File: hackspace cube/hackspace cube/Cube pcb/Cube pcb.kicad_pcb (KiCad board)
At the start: 2 copper layers, 57 parts, among them J1 Conn_01x08 ( conector 1), J2 Conn_01x08 ( conector 2), J3 Conn_01x02 ( exstra ground co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, J4 Conn_01x14 ( Spare Ports ), Q1 BSS138, Q10 BSS138, Q11 BSS138, Q12 BSS138, Q13 BSS138, Q14 BSS138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

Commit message: updating pcb
updating pcb most pins attached
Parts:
- moved C2 126.9 mm to (170.4, 108.5), turned to 180 degrees
- moved C1 122.3 mm to (166.1, 108.5)
- moved R24 101.7 mm to (139.7, 125.0)
- moved R23 100.9 mm to (139.7, 114.5)
- moved R22 97.3 mm to (134.2, 125.0)
- moved R21 96.5 mm to (134.7, 114.5)
- moved R20 93.8 mm to (129.2, 125.0)
- moved R19 92.0 mm to (129.2, 114.5)
- moved R18 90.7 mm to (123.9, 125.0)
- moved R17 88.0 mm to (123.6, 114.5)
- moved R26 75.7 mm to (112.1, 125.0)
- moved R25 72.8 mm to (112.1, 114.5)
- moved R28 68.3 mm to (106.6, 125.0)
- moved R27 65.8 mm to (106.6, 114.5)
- moved R30 61.5 mm to (101.6, 125.0)
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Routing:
- net +3.3V: track 77.6 -> 283.4 mm, vias 1 -> 0
- net +5V: track 61.0 -> 226.2 mm
- net GPIO-11: track 0.00 -> 118.8 mm, vias 0 -> 1
- net GPIO-10: track 0.00 -> 107.9 mm, vias 0 -> 2
- net GPIO-9: track 0.00 -> 107.4 mm, vias 0 -> 2
- net GPIO-12: track 0.00 -> 102.4 mm, vias 0 -> 2
- net GPIO-8: track 0.00 -> 96.2 mm, vias 0 -> 2
- net GPIO-4: track 12.7 -> 103.7 mm, vias 0 -> 1
- net GPIO-13: track 0.00 -> 90.0 mm, vias 0 -> 2
- net DATA-13: track 0.00 -> 89.5 mm, vias 0 -> 1
- net GPIO-1: track 11.4 -> 99.6 mm
- net GPIO-2: track 11.0 -> 98.5 mm
- net GPIO-5: track 12.3 -> 95.1 mm
- net GPIO-3: track 16.9 -> 98.4 mm
- net DATA-14: track 0.00 -> 79.5 mm, vias 0 -> 1
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
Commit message: pcb first draft
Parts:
- moved C3 23.6 mm to (113.5, 106.5), turned to 180 degrees
- moved C4 4.90 mm to (94.5, 107.0)
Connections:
- J4 pad 10: GPIO-16 -> GPIO-20
- J4 pad 11: GPIO-28 -> GPIO-19
- J4 pad 12: GPIO-27 -> GPIO-18
- J4 pad 13: GPIO-26 -> GPIO-17
- J4 pad 14: ADC_VREF -> GPIO-16
- J4 pad 2: RUN -> 3V3_EN
- J4 pad 3: 3V3_EN -> ADC_VREF
- J4 pad 4: GPIO-22 -> GPIO-28
- J4 pad 5: GPIO-21 -> GPIO-27
- J4 pad 6: GPIO-20 -> GPIO-26
- J4 pad 7: GPIO-19 -> RUN
- J4 pad 8: GPIO-18 -> GPIO-22
- J4 pad 9: GPIO-17 -> GPIO-21
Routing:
- net VSYS: track 0.00 -> 15.9 mm
- net 3V3_EN: track 0.00 -> 13.2 mm
- net GPIO-28: track 0.00 -> 9.58 mm
- net ADC_VREF: track 0.00 -> 9.58 mm
- net RUN: track 0.00 -> 7.89 mm
- net GPIO-27: track 0.00 -> 7.89 mm
- net GPIO-26: track 0.00 -> 7.89 mm
- net GPIO-22: track 0.00 -> 7.89 mm
- net GPIO-20: track 0.00 -> 6.84 mm
- net GPIO-19: track 0.00 -> 6.84 mm
- net GPIO-18: track 0.00 -> 6.84 mm
- net GPIO-21: track 0.00 -> 6.84 mm
- net GPIO-17: track 0.00 -> 6.68 mm
- net GPIO-16: track 0.00 -> 6.68 mm
- net GND: track 7.66 -> 10.9 mm, vias 0 -> 2
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
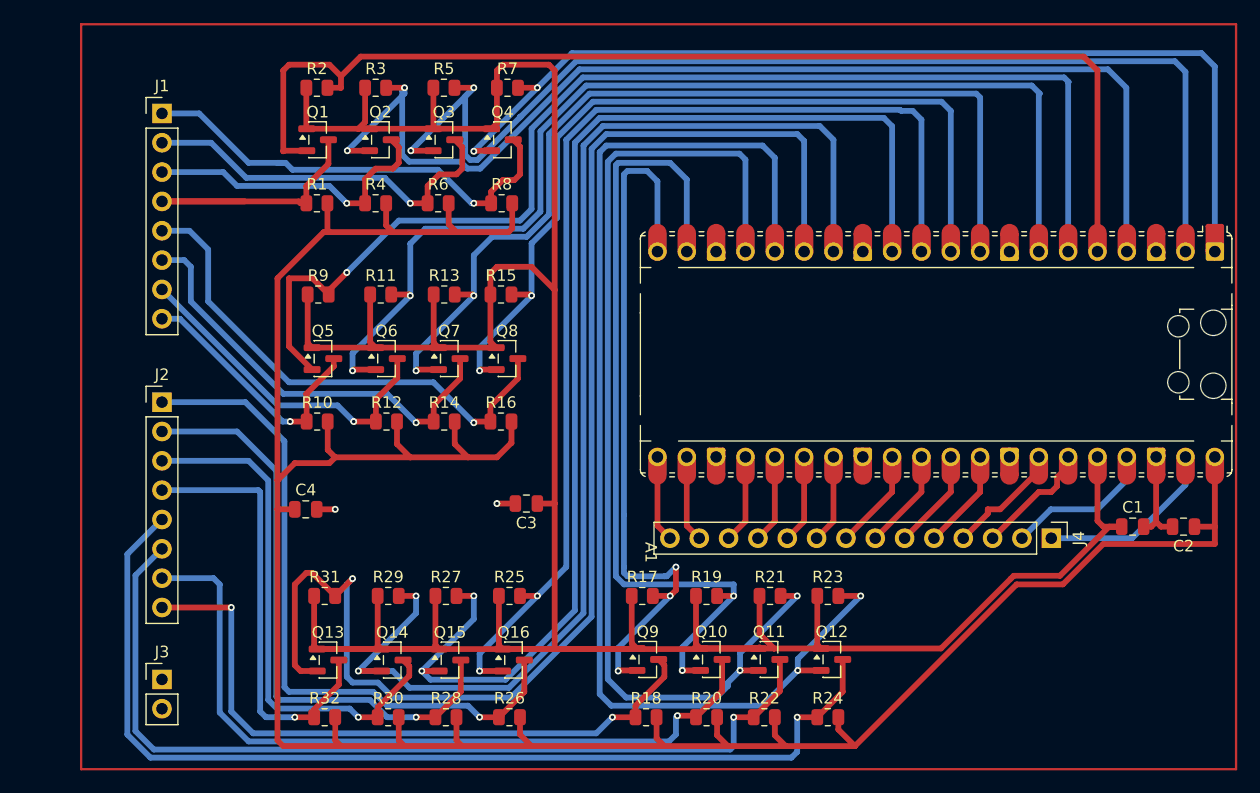
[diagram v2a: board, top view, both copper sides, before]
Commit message: update pcb
i have added labels and basic info onto the pcb
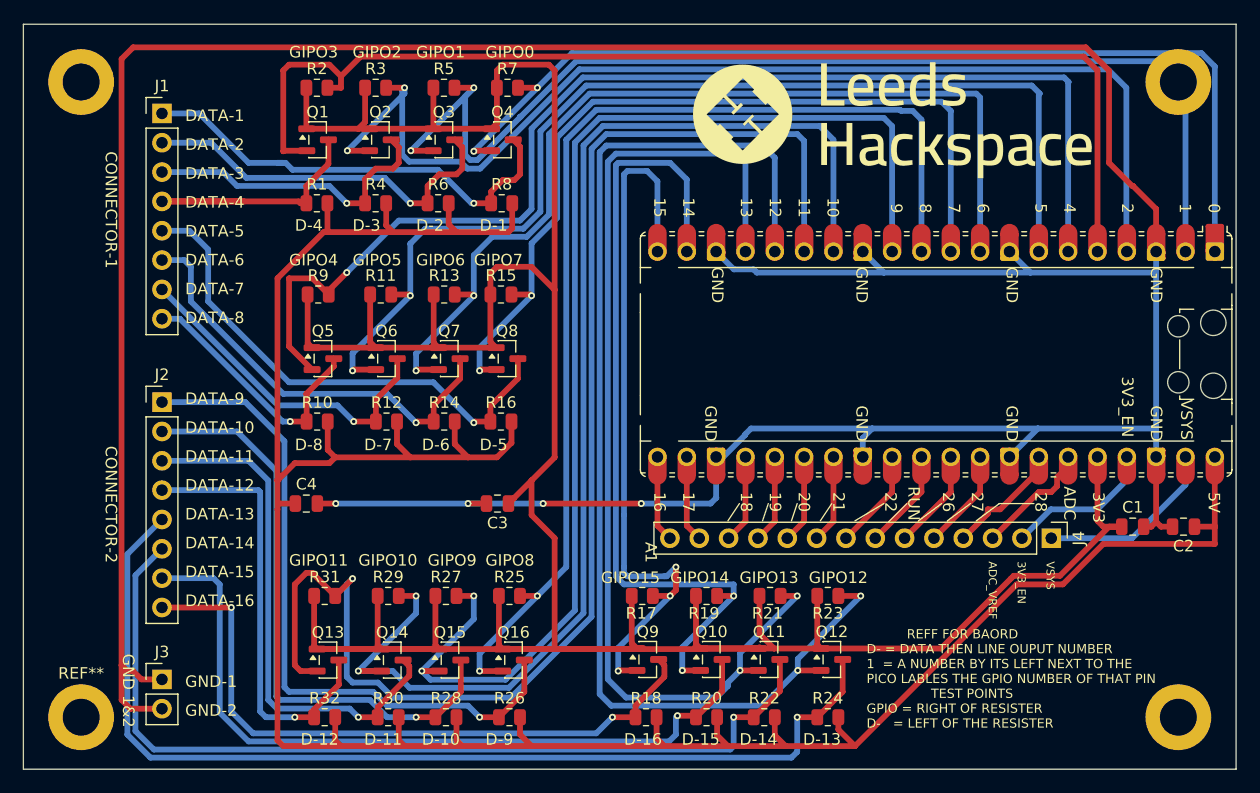
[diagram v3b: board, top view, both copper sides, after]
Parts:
- added ?: , , F.Cu at (170.0, 125.0)
- added ?: , , F.Cu at (75.0, 70.0)
- added ?: , , F.Cu at (170.0, 70.0)
- added REF**: MountingHole_3.2mm_M3_ISO7380_Pad, MountingHole:MountingHole_3.2mm_M3_ISO7380_Pad, F.Cu at (75.0, 125.0)
- moved C3 2.50 mm to (111.0, 106.5)
- moved C4 0.50 mm to (94.5, 106.5)
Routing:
- net GND: track 10.9 -> 321.5 mm, vias 2 -> 4
- net +3.3V: track 284.9 -> 287.8 mm
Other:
- board outline added: 105 x 64.5 mm
- board text added: "0"
- board text added: "1"
- board text added: "10"
- board text added: "11"
- board text added: "12"
- board text added: "13"
- board text added: "14"
- board text added: "15"
- board text added: "16"
- board text added: "17"
- board text added: "18"
- board text added: "19"
- board text added: "2"
- board text added: "20"
- board text added: "21"
- board text added: "22"
- board text added: "26"
- board text added: "27"
- board text added: "28"
- board text added: "3V3"
- board text added: "3V3_EN"
- board text added: "4"
- board text added: "5"
- board text added: "5V"
- board text added: "6"
- board text added: "7"
- board text added: "8"
- board text added: "9"
- board text added: "ADC"
- board text added: "ADC_VREF"
- board text added: "CONNECTOR-1"
- board text added: "CONNECTOR-2"
- board text added: "D-1"
- board text added: "D-10"
- board text added: "D-11"
- board text added: "D-12"
- board text added: "D-13"
- board text added: "D-14"
- board text added: "D-15"
- board text added: "D-16"
- board text added: "D-2"
- board text added: "D-3"
- board text added: "D-4"
- board text added: "D-5"
- board text added: "D-6"
- board text added: "D-7"
- board text added: "D-8"
- board text added: "D-9"
- board text added: "DATA-1"
- board text added: "DATA-10"
- board text added: "DATA-11"
- board text added: "DATA-12"
- board text added: "DATA-13"
- board text added: "DATA-14"
- board text added: "DATA-15"
- board text added: "DATA-16"
- board text added: "DATA-2"
- board text added: "DATA-3"
- board text added: "DATA-4"
- board text added: "DATA-5"
- board text added: "DATA-6"
- board text added: "DATA-7"
- board text added: "DATA-8"
- board text added: "DATA-9"
- board text added: "GIPO0"
- board text added: "GIPO1"
- board text added: "GIPO10"
- board text added: "GIPO11"
- board text added: "GIPO12"
- board text added: "GIPO13"
- board text added: "GIPO14"
- board text added: "GIPO15"
- board text added: "GIPO2"
- board text added: "GIPO3"
- board text added: "GIPO4"
- board text added: "GIPO5"
- board text added: "GIPO6"
- board text added: "GIPO7"
- board text added: "GIPO8"
- board text added: "GIPO9"
- board text added: "GND"
- board text added: "GND 1&2"
- board text added: "GND-1"
- board text added: "GND-2"
- board text added: "PCB DESIGNED BY SAMSON B CAN BE FOUND ON GITHUB AT https://github.com/bozzer91 IF NOT ON LEEDS HACKSPACE GITHUB LICENCE: OPEN SOURCE"
- board text added: "REFF FOR BAORD D- = DATA THEN LINE OUPUT NUMBER 1 = A NUMBER BY ITS LEFT NEXT TO THE PICO LABLES THE GPIO NUMBER OF THAT PIN TEST POINTS GPIO = RIGHT OF RESISTER D- = LEFT OF THE RESISTER"
- board text added: "RUN"
- board text added: "THE CUBE FOR DRIVING LEDS"
- board text added: "VSYS"

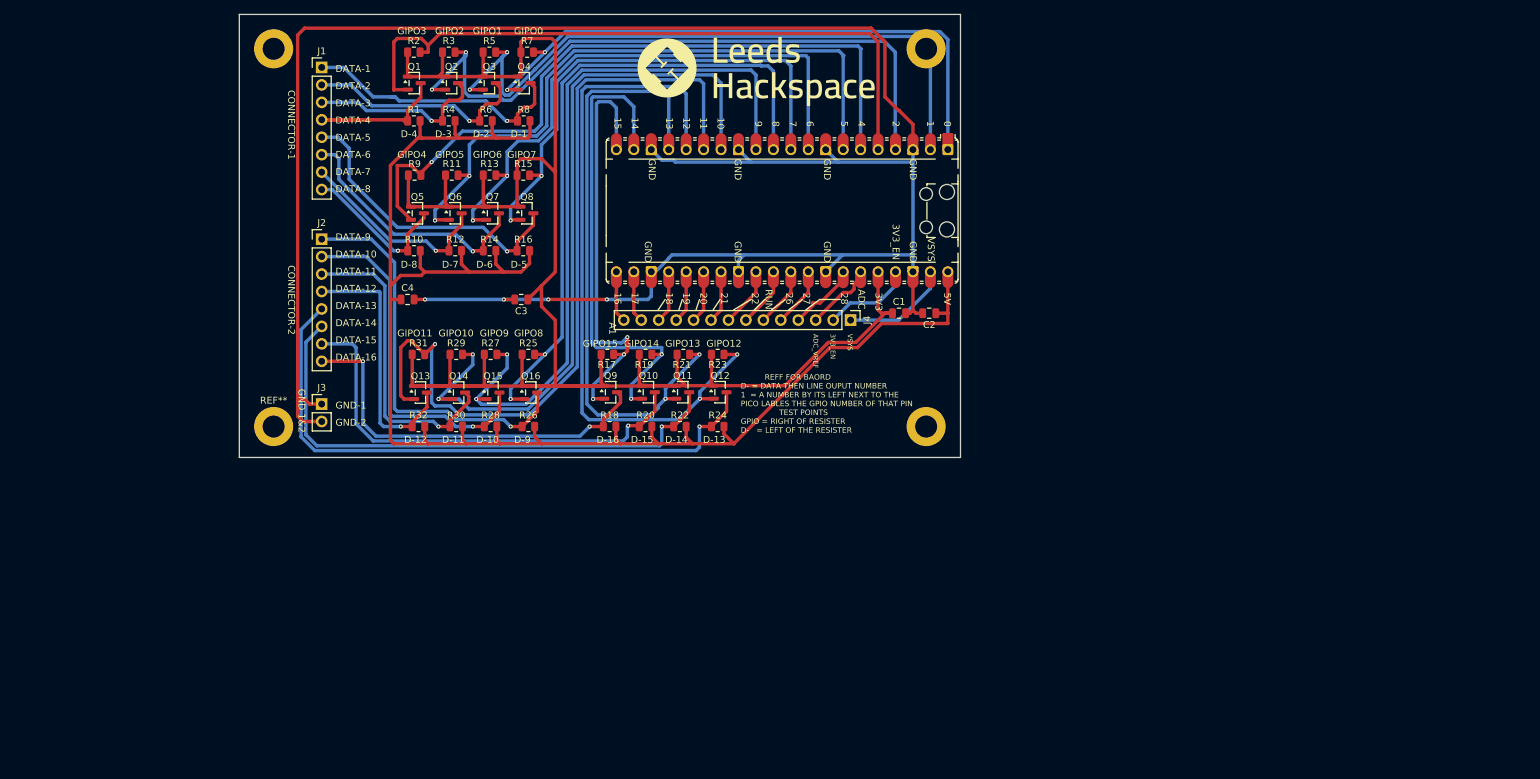
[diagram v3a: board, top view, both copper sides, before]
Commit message: updated wiring D and PCB
 wiring D now has GND on the connector pins . PCB now has new shorter design to make it 10cm wide just need to add ground plain
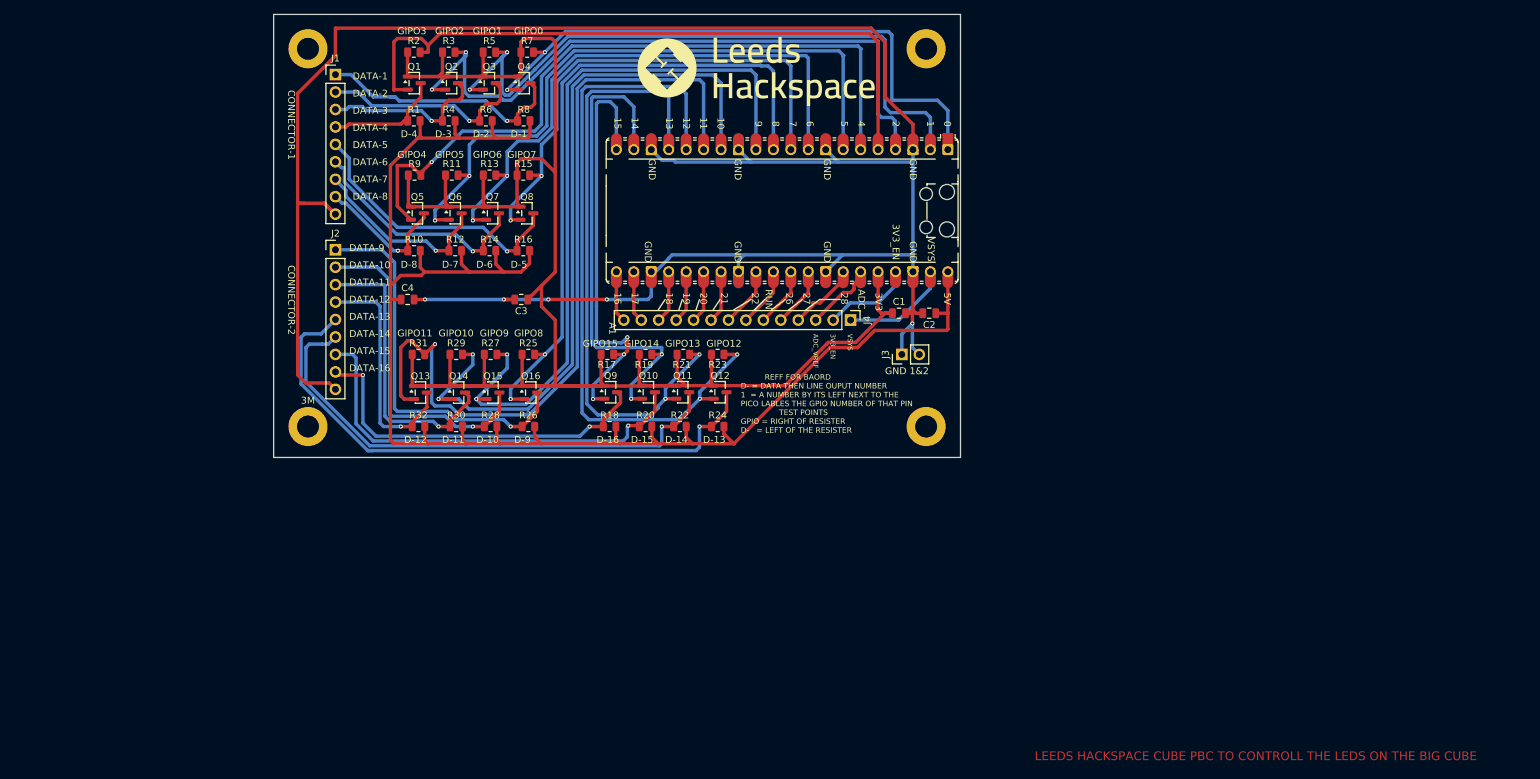
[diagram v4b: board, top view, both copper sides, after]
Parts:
- J1: value Conn_01x08 ( conector 1) -> Conn_01x09 ( conector 1); footprint Connector_PinHeader_2.54mm:PinHeader_1x08_P2.54mm_Vertical -> Connector_PinHeader_2.54mm:PinHeader_1x09_P2.54mm_Vertical
- J2: value Conn_01x08 ( conector 2) -> Conn_01x09 ( conector 2); footprint Connector_PinHeader_2.54mm:PinHeader_1x08_P2.54mm_Vertical -> Connector_PinHeader_2.54mm:PinHeader_1x09_P2.54mm_Vertical
- moved J3 84.8 mm to (166.5, 114.5), turned to 90 degrees
- moved 3M 5.00 mm to (80.0, 125.0)
- moved ? 5.00 mm to (80.0, 70.0)
- moved J2 2.52 mm to (84.0, 99.3)
- moved J1 2.25 mm to (84.0, 73.8)
- renumbered REF** to 3M
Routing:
- net GND: track 321.5 -> 332.2 mm, vias 4 -> 5
- net DATA-4: track 26.0 -> 17.2 mm
- net DATA-16: track 57.6 -> 53.8 mm
- net DATA-12: track 38.3 -> 34.5 mm
- net DATA-14: track 79.5 -> 75.9 mm
- net DATA-15: track 66.4 -> 62.9 mm
- net DATA-5: track 44.4 -> 41.2 mm
- net DATA-13: track 89.5 -> 86.5 mm
- net DATA-9: track 58.8 -> 56.2 mm
- net DATA-11: track 45.3 -> 42.7 mm
- net DATA-10: track 51.2 -> 48.6 mm
- net DATA-1: track 39.6 -> 37.2 mm
- net DATA-2: track 33.1 -> 30.6 mm
- net DATA-6: track 37.6 -> 35.1 mm
- net DATA-3: track 26.6 -> 24.5 mm
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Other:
- board size 105 x 64.5 mm -> 100 x 64.5 mm
- board text added: "1.3"
- board text added: "CUBE CONTROLL BAORD pcb"
- board text added: "LEEDS HACKSPACE CUBE PBC TO CONTROLL THE LEDS ON THE BIG CUBE"
- board text added: "PCB DESIGNED BY SAMSON B LEEDS HACKSPACE CUBE CONTROLL BAORD CAN BE FOUND ON GITHUB AT www.github.com/bozzer91 IF NOT ON LEEDS HACKSPACE GITHUB LICENCE: OPEN SOURCE"
- board text added: "one"
- board text removed: "GND-1"
- board text removed: "GND-2"
- board text removed: "PCB DESIGNED BY SAMSON B CAN BE FOUND ON GITHUB AT https://github.com/bozzer91 IF NOT ON LEEDS HACKSPACE GITHUB LICENCE: OPEN SOURCE"

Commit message: rev 1.4
added new smooth caps and updated pcb
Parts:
- added C10: 100nF, Capacitor_SMD:C_0805_2012Metric, F.Cu at (145.0, 116.0)
- added C5: 100nF, Capacitor_SMD:C_0805_2012Metric, F.Cu at (117.0, 125.0)
- added C6: 100nF, Capacitor_SMD:C_0805_2012Metric, F.Cu at (117.0, 121.0)
- added C7: 100nF, Capacitor_SMD:C_0805_2012Metric, F.Cu at (114.5, 83.0)
- added C8: 100nF, Capacitor_SMD:C_0805_2012Metric, F.Cu at (117.5, 71.5)
- added C9: 100nF, Capacitor_SMD:C_0805_2012Metric, F.Cu at (144.0, 122.0)
- C1, C2, C3, C4: value C -> 100nF
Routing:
- net GND: track 332.2 -> 449.5 mm, vias 5 -> 10
- net +5V: track 228.2 -> 235.8 mm
- net +3.3V: track 287.8 -> 294.0 mm
